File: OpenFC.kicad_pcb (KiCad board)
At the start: 6 copper layers, 29.5 x 29.1 mm, 170 parts, among them J1 5V, J10 5V, J11 5V, J12 5V, J13 5V, J14 5V, J15 5V, J16 5V, J17 5V, J18 5V, J19 5V, J2 5V, J20 5V, J21 5V, J22 5V, J23 5V, J24 5V, J25 5V, J26 5V, J27 5V, J28 5V, J29 5V, J3 5V, J30 5V, J31 5V, J32 5V, J33 5V, J34 5V, J35 5V, J36 5V, J37 5V, J38 5V, J39 5V, J4 5V, J40 5V, J41 5V, J42 5V, J43 5V, J44 5V, J45 5V, J46 5V, J47 5V, J48 5V, J5 5V, J53 5V, J54 5V, J55 5V, J56 5V, J57 5V, J59 5V, J6 5V, J7 5V, J8 5V, J9 5V, P1 SM08B-SRSS-TB(LF)(SN), Q7 DMN1150UFB-7B, SW1 B3U-1000P, U1 SM06B-SRSS-TB(LF)(SN), U10 TLV75533PDBVR, U11 RP2350A_C42411118, U12 ABM8-272-T3_C20625731, U13 W25Q32RVXHJQ TR, U14 LSM6DSV16XTR, U15 XL-1010RGBC-WS2812B, U16 XL-1010RGBC-WS2812B, U17 XL-1010RGBC-WS2812B, U18 XL-1010RGBC-WS2812B, U19 ESP8285H16, U2 W25Q128JVPIQTR, U20 SX1281IMLTRT, U3 XL-1010RGBC-WS2812B, U4 XL-1010RGBC-WS2812B, U5 XL-1010RGBC-WS2812B, U6 LMR51420YDDCR, U7 LMR51420YDDCR, U8 XL-1010RGBC-WS2812B, U9 TLV75533PDBVR, X1 XTM20026000FT00351005

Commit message: First routing
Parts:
- removed D2, D4: LED_1_Green, LED_SMD:LED_0603_1608Metric
- removed J10, J12, J54, J55, J56, J57, J9: 5V, lib:small_pad
- removed R4, R53: 30R, Resistor_SMD:R_0402_1005Metric
- D18, R32: moved to F.Cu
- D3, R3: moved to B.Cu
- moved D1 60.5 mm to (56.8, 102.8)
- moved R29 58.0 mm to (56.4, 104.5), turned to 90 degrees
- moved C40 53.5 mm to (65.0, 107.8), turned to -90 degrees
- moved D3 50.2 mm to (69.4, 122.3), turned to 90 degrees
- moved R3 49.7 mm to (69.7, 119.8), turned to 90 degrees
- moved R32 47.6 mm to (69.1, 107.2)
- moved U17 40.3 mm to (73.6, 124.3), turned to -155 degrees
- moved U18 37.9 mm to (75.9, 121.9), turned to 155 degrees
- moved U3 36.5 mm to (75.9, 101.0), turned to 25 degrees
- moved U4 33.3 mm to (73.6, 98.6), turned to -25 degrees
- moved J40 31.7 mm to (62.0, 105.0), turned to 90 degrees
- moved U15 30.3 mm to (50.2, 121.9), turned to -155 degrees
- moved U16 30.2 mm to (52.6, 124.3), turned to 155 degrees
- moved J8 29.3 mm to (53.0, 118.5)
- moved J7 29.2 mm to (53.0, 116.5)
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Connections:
- U11 pad 4: /RP2350A/ESP8285_EN -> /ELRS/ESP8285_EN
- U11 pad 5: /RP2350A/ESP8285_RST -> /ELRS/ESP8285_RST
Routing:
- net +4.5V: track 0.00 -> 63.5 mm, vias 0 -> 19
- net +BATT: track 0.00 -> 60.4 mm, vias 0 -> 18
- net /LED: track 0.00 -> 59.6 mm, vias 0 -> 6
- net /UART1_RX: track 0.50 -> 53.8 mm, vias 0 -> 2
- net /UART1_TX: track 0.00 -> 47.5 mm, vias 0 -> 3
- net GND: track 3.83 -> 49.1 mm, vias 1 -> 98
- net +3.3V: track 23.7 -> 66.2 mm, vias 6 -> 27
- net +12V: track 0.00 -> 39.7 mm, vias 0 -> 9
- net +1.1V: track 6.68 -> 39.4 mm, vias 1 -> 5
- net /PADS/M4: track 0.00 -> 32.4 mm, vias 0 -> 4
- net /PADS/M2: track 0.00 -> 31.1 mm, vias 0 -> 2
- net /PADS/CURRENT: track 0.00 -> 30.9 mm, vias 0 -> 3
- net /PADS/ESC_TELEM: track 0.00 -> 29.1 mm, vias 0 -> 4
- net /ELRS/ESP8285_RST: track 1.05 -> 28.6 mm, vias 0 -> 3
- net /PADS/M3: track 0.00 -> 26.4 mm, vias 0 -> 4
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- added copper zone on B.Cu, net +12V
- added copper zone on In3.Cu, net +12V
- added copper zone on In4.Cu, net +12V
- added copper zone on B.Cu, net +3.3V
- added copper zone on In4.Cu, net +3.3V
- added copper zone on In3.Cu, net +4.5V
- added copper zone on B.Cu, net +5V
- added copper zone on In2.Cu, net +5V
- added copper zone on B.Cu, net +BATT
- added copper zone on F.Cu, net +BATT
- added copper zone on B.Cu, net GND
- added copper zone on F.Cu, net GND
- added copper zone on In1.Cu, net GND
- added copper zone on In2.Cu, net GND
- added copper zone on In3.Cu, net GND
- added copper zone on In4.Cu, net GND
- added copper zone on B.Cu, net Net-(U6-SW)
- added copper zone on B.Cu, net Net-(U7-SW)
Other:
- outline, holes or cut-outs redrawn

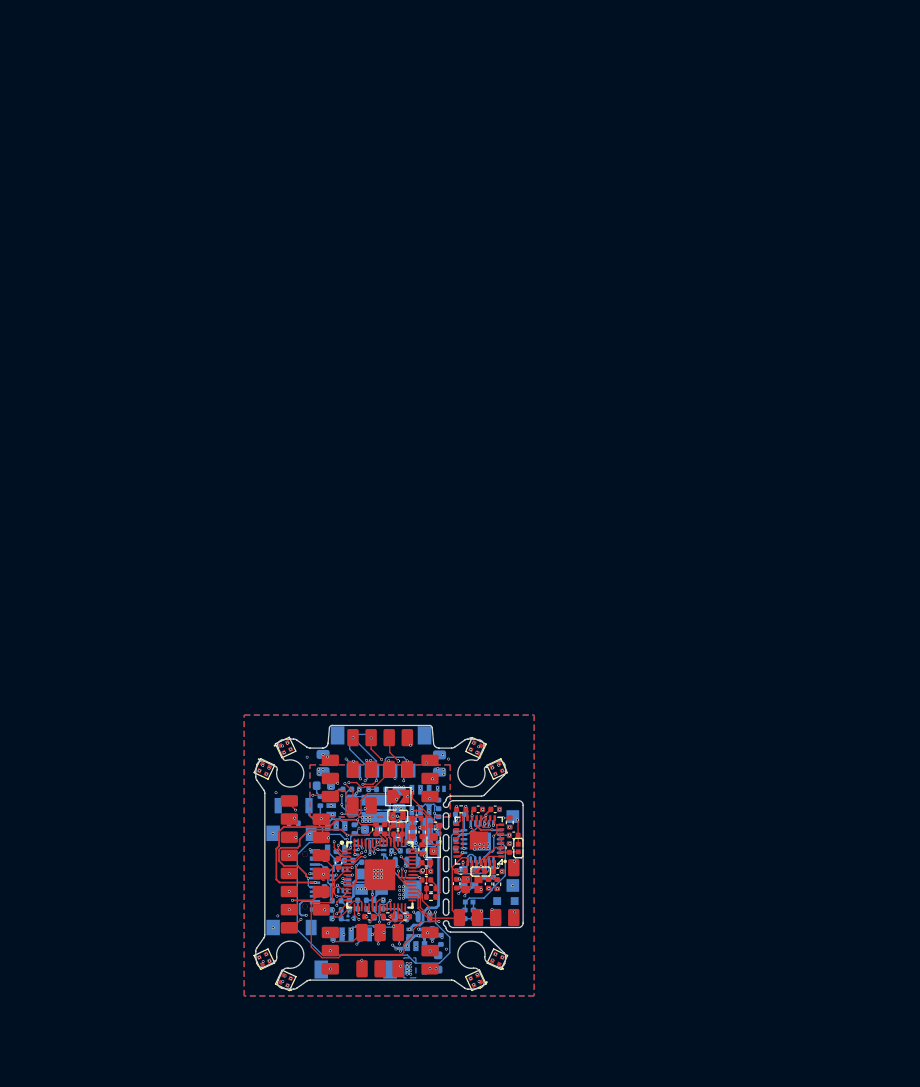
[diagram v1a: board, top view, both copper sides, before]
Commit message: Revised routing. All logic is routed just need uart and power planes
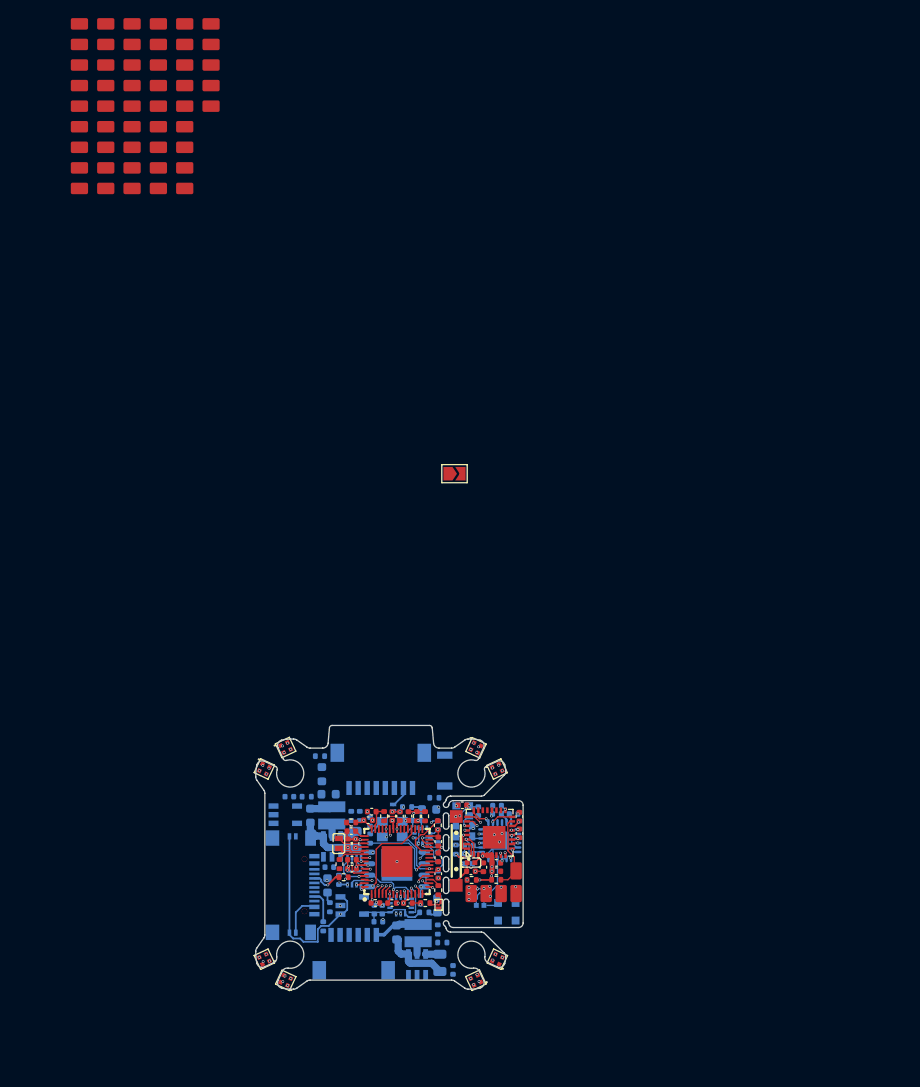
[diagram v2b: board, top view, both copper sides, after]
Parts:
- removed C107: 100n, Capacitor_SMD:C_0402_1005Metric
- removed C16: 4.7uF 50v, Capacitor_SMD:C_0805_2012Metric
- added C111: 100n, Capacitor_SMD:C_0402_1005Metric, B.Cu at (69.4, 107.2)
- added D2: LED_1_Green, LED_SMD:LED_0603_1608Metric, B.Cu at (68.4, 105.4)
- added D4: LED_1_Green, LED_SMD:LED_0603_1608Metric, B.Cu at (69.3, 116.0)
- added J10: 5V, lib:small_pad, F.Cu at (32.7, 18.7)
- added J12: 5V, lib:small_pad, F.Cu at (32.7, 23.3)
- added J54: 5V, lib:small_pad, F.Cu at (44.3, 18.7)
- added J55: 5V, lib:small_pad, F.Cu at (44.3, 21.0)
- added J56: 5V, lib:small_pad, F.Cu at (44.3, 23.3)
- added J57: 5V, lib:small_pad, F.Cu at (44.3, 25.5)
- added J58: 5V, lib:small_pad, F.Cu at (44.3, 27.8)
- added J9: 5V, lib:small_pad, F.Cu at (29.8, 36.9)
- added R4: 30R, Resistor_SMD:R_0402_1005Metric, B.Cu at (67.9, 116.8)
- added R53: 30R, Resistor_SMD:R_0402_1005Metric, B.Cu at (66.0, 105.2)
- added U30: BMP388, lib:SENSORM-SMD_BMP388, B.Cu at (67.7, 108.3)
- C100, C46, C47, C48, C8, C97, C98, C99, L13, Q7, R40, R49, R5: moved to F.Cu
- C13, C18, D18, L8, R1, R2, R32, R7, X1: moved to B.Cu
- moved J28 106.7 mm to (38.5, 18.7), turned to 0 degrees
- moved J29 104.9 mm to (38.5, 21.0), turned to 0 degrees
- moved J19 104.6 mm to (35.6, 18.7)
- moved J20 104.3 mm to (35.6, 21.0)
- moved J35 101.0 mm to (38.5, 25.5), turned to 0 degrees
- moved J30 97.6 mm to (38.5, 23.3)
- moved J41 97.0 mm to (41.4, 18.7), turned to 0 degrees
- moved J16 95.6 mm to (32.7, 32.3), turned to 0 degrees
- moved J17 95.4 mm to (32.7, 34.6), turned to 0 degrees
- moved J36 95.0 mm to (38.5, 27.8), turned to 0 degrees
- moved J42 92.7 mm to (41.4, 21.0), turned to 0 degrees
- moved J37 92.2 mm to (38.5, 30.1), turned to 0 degrees
- moved J18 89.6 mm to (32.7, 36.9), turned to 0 degrees
- moved J38 89.5 mm to (38.5, 32.3), turned to 0 degrees
- moved J11 88.7 mm to (32.7, 21.0)
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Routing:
- net /LED: track 59.6 -> 0.00 mm, vias 6 -> 0
- net +BATT: track 60.4 -> 5.78 mm, vias 18 -> 0
- net /UART1_RX: track 53.8 -> 9.88 mm
- net +4.5V: track 63.5 -> 21.7 mm, vias 19 -> 9
- net /UART1_TX: track 47.5 -> 10.8 mm, vias 3 -> 2
- net +12V: track 39.7 -> 4.45 mm, vias 9 -> 0
- net +1.1V: track 39.4 -> 7.66 mm, vias 5 -> 3
- net /PADS/M4: track 32.4 -> 0.85 mm, vias 4 -> 1
- net /PADS/CURRENT: track 30.9 -> 0.00 mm, vias 3 -> 1
- net /PADS/M2: track 31.1 -> 0.46 mm, vias 2 -> 1
- net /PADS/ESC_TELEM: track 29.1 -> 0.00 mm, vias 4 -> 0
- net +3.3V: track 66.2 -> 38.4 mm, vias 27 -> 25
- net /PADS/M3: track 26.4 -> 0.41 mm, vias 4 -> 1
- net /PADS/M1: track 25.3 -> 1.02 mm, vias 4 -> 1
- net /PADS/PIOUART0_RX: track 23.4 -> 0.00 mm, vias 2 -> 0
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- removed copper zone on B.Cu, net +12V
- removed copper zone on In3.Cu, net +12V
- removed copper zone on In4.Cu, net +12V
- removed copper zone on B.Cu, net +3.3V
- removed copper zone on In4.Cu, net +3.3V
- removed copper zone on In3.Cu, net +4.5V
- removed copper zone on B.Cu, net +5V
- removed copper zone on In2.Cu, net +5V
- removed copper zone on B.Cu, net +BATT
- removed copper zone on F.Cu, net +BATT
- removed copper zone on B.Cu, net GND
- removed copper zone on F.Cu, net GND
- removed copper zone on In1.Cu, net GND
- removed copper zone on In2.Cu, net GND
- removed copper zone on In3.Cu, net GND
- removed copper zone on In4.Cu, net GND
- removed copper zone on B.Cu, net Net-(U6-SW)
- removed copper zone on B.Cu, net Net-(U7-SW)
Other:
- copper layers 6 -> 8

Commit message: almost finished routing
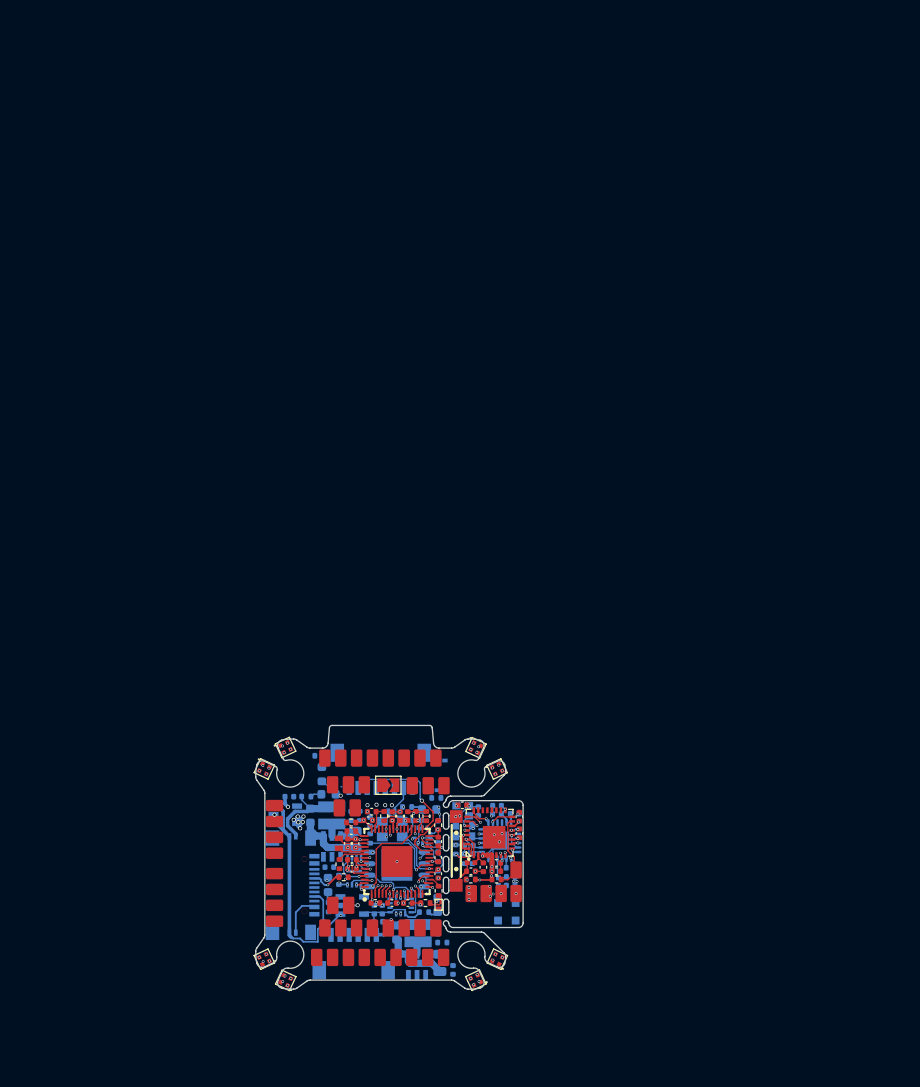
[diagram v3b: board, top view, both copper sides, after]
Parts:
- removed C108: 100nF, Capacitor_SMD:C_0402_1005Metric
- removed C6: 10nF, Capacitor_SMD:C_0402_1005Metric
- removed D18: LED_1_Green, LED_SMD:LED_0603_1608Metric
- removed J10, J11, J12, J54, J55, J58, J9: 5V, lib:small_pad
- removed R27, R30: 100k, Resistor_SMD:R_0402_1005Metric
- removed R32: 200, Resistor_SMD:R_0402_1005Metric
- removed R40, R51: 10k, Resistor_SMD:R_0402_1005Metric
- removed R43, R49: 1k, Resistor_SMD:R_0402_1005Metric
- removed SW1: B3U-1000P, lib:KEY-SMD_B3U-1000PM
- added C1: 10nF, Capacitor_SMD:C_0402_1005Metric, B.Cu at (77.8, 105.9)
- added C2: 100n, Capacitor_SMD:C_0402_1005Metric, F.Cu at (66.0, 106.2)
- added D5: LED_1_Green, LED_SMD:LED_0603_1608Metric, B.Cu at (57.2, 113.8)
- added R10: 10k, Resistor_SMD:R_0402_1005Metric, F.Cu at (69.4, 107.2)
- added R11: 10k, Resistor_SMD:R_0402_1005Metric, F.Cu at (67.0, 106.2)
- added R12: 10k, Resistor_SMD:R_0402_1005Metric, B.Cu at (69.2, 104.2)
- added R13: 1k, Resistor_SMD:R_0402_1005Metric, F.Cu at (69.5, 114.4)
- added R14: 100k, Resistor_SMD:R_0402_1005Metric, B.Cu at (69.4, 118.7)
- added R15: 200R, Resistor_SMD:R_0402_1005Metric, B.Cu at (54.9, 104.0)
- added R16: 100k, Resistor_SMD:R_0402_1005Metric, B.Cu at (59.8, 106.2)
- added R9: 10k, Resistor_SMD:R_0402_1005Metric, B.Cu at (77.4, 111.8)
- added U21: TS2306A 240GF MSM 9_C2976675, lib:SW-SMD_4P-L3.0-W2.0-P0.85-LS3.5, B.Cu at (69.7, 101.7)
- R3, R4: value 30R -> 33R
- moved J19 108.6 mm to (70.0, 121.8), turned to -90 degrees
- moved J28 106.3 mm to (64.8, 121.8), turned to -90 degrees
- moved J20 105.9 mm to (68.2, 121.8), turned to -90 degrees
- moved J29 103.7 mm to (63.0, 121.8), turned to -90 degrees
- moved J21 103.2 mm to (66.5, 121.8), turned to -90 degrees
- moved J41 102.3 mm to (63.9, 118.5), turned to 90 degrees
- moved J42 100.5 mm to (65.7, 118.5), turned to 90 degrees
- moved J35 98.9 mm to (61.2, 121.8), turned to -90 degrees
- moved J43 98.7 mm to (67.4, 118.5), turned to 90 degrees
- moved J30 97.7 mm to (60.4, 118.5), turned to 90 degrees
- moved J44 97.0 mm to (69.2, 118.5), turned to 90 degrees
- moved J36 96.3 mm to (59.5, 121.8), turned to -90 degrees
- moved J22 95.4 mm to (56.9, 118.5), turned to 90 degrees
- moved J37 93.7 mm to (57.8, 121.8), turned to -90 degrees
- moved J23 93.6 mm to (58.7, 118.5), turned to 90 degrees
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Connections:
- J59 pad 1: /ELRS/ESP8285_RST -> /ELRS/ESP_BOOT0
- R29 pad 2: Net-(D1-A) -> Net-(D5-A)
- R3 pad 1: Net-(D3-A) -> +3.3V
- R3 pad 2: +3.3V -> Net-(D3-A)
- R4 pad 1: Net-(D4-A) -> +3.3V_GYRO
- R4 pad 2: +3.3V_GYRO -> Net-(D4-A)
- R6 pad 2: /ELRS/ESP8285_RST -> /ELRS/ESP8285_EN
- R8 pad 2: /ELRS/ESP8285_EN -> /ELRS/ESP_BOOT0
- U11 pad 5: /ELRS/ESP8285_RST -> /ELRS/ESP_BOOT0
- U19 pad 15: /ELRS/ESP8285_RST -> /ELRS/ESP_BOOT0
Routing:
- net /PADS/M4: track 0.85 -> 22.8 mm, vias 1 -> 2
- net +4.5V: track 21.7 -> 39.1 mm
- net /PADS/M3: track 0.41 -> 15.8 mm, vias 1 -> 2
- net /PADS/ESC_TELEM: track 0.00 -> 14.0 mm, vias 0 -> 1
- net /PADS/M2: track 0.46 -> 13.2 mm, vias 1 -> 2
- net GND: track 55.6 -> 67.5 mm, vias 58 -> 60
- net /PADS/M1: track 1.02 -> 11.3 mm, vias 1 -> 2
- net /UART1_TX: track 10.8 -> 20.3 mm, vias 2 -> 3
- net /ELRS/ESP_BOOT0: track 0.00 -> 9.26 mm, vias 0 -> 1
- net /ELRS/ESP8285_RST: track 9.26 -> 0.00 mm, vias 1 -> 0
- net /UART1_RX: track 9.88 -> 17.4 mm, vias 2 -> 3
- net +5V: track 2.44 -> 9.42 mm
- net +3.3V: track 38.4 -> 42.6 mm, vias 25 -> 32
- net Net-(U20-RFIO): track 6.89 -> 3.13 mm
- net +BATT: track 5.78 -> 7.19 mm
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- added copper zone on In1.Cu, net GND
- added copper zone on In6.Cu, net GND

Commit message: Final routing
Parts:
- removed J56: 5V, lib:small_pad
- added J9: 5V, lib:small_pad, F.Cu at (54.2, 109.2)
- added U22: XL-1010RGBC-WS2812B, lib:LED-SMD_4P-L1.0-W1.0-TL_XL-1010RGBC-WS2812B, B.Cu at (75.9, 101.0)
- added U23: XL-1010RGBC-WS2812B, lib:LED-SMD_4P-L1.0-W1.0-TL_XL-1010RGBC-WS2812B, B.Cu at (73.6, 98.6)
- added U24: XL-1010RGBC-WS2812B, lib:LED-SMD_4P-L1.0-W1.0-TL_XL-1010RGBC-WS2812B, B.Cu at (52.6, 98.6)
- added U25: XL-1010RGBC-WS2812B, lib:LED-SMD_4P-L1.0-W1.0-TL_XL-1010RGBC-WS2812B, B.Cu at (50.2, 100.9)
- added U26: XL-1010RGBC-WS2812B, lib:LED-SMD_4P-L1.0-W1.0-TL_XL-1010RGBC-WS2812B, B.Cu at (50.2, 122.0)
- added U27: XL-1010RGBC-WS2812B, lib:LED-SMD_4P-L1.0-W1.0-TL_XL-1010RGBC-WS2812B, B.Cu at (52.6, 124.3)
- added U28: XL-1010RGBC-WS2812B, lib:LED-SMD_4P-L1.0-W1.0-TL_XL-1010RGBC-WS2812B, B.Cu at (73.6, 124.3)
- added U29: XL-1010RGBC-WS2812B, lib:LED-SMD_4P-L1.0-W1.0-TL_XL-1010RGBC-WS2812B, B.Cu at (75.9, 121.9)
- moved J6 13.1 mm to (51.2, 118.1), turned to 0 degrees
- moved J48 13.0 mm to (51.2, 104.8), turned to 180 degrees
- moved J5 9.60 mm to (51.2, 116.3), turned to 0 degrees
- moved J47 9.45 mm to (51.2, 106.5), turned to 180 degrees
- moved J57 6.47 mm to (54.1, 107.4), turned to 180 degrees
- moved J7 6.10 mm to (51.2, 114.6), turned to 180 degrees
- moved J46 5.95 mm to (51.2, 108.3), turned to 180 degrees
- moved J40 5.90 mm to (54.1, 113.7), turned to 180 degrees
- moved C36 5.79 mm to (65.2, 123.2)
- moved J39 3.72 mm to (54.1, 115.5), turned to 180 degrees
- moved J8 2.60 mm to (51.2, 112.8), turned to 180 degrees
- moved J45 2.45 mm to (51.2, 110.0), turned to 180 degrees
- moved J22 1.90 mm to (57.0, 120.4)
- moved J23 1.90 mm to (58.8, 120.4)
- moved J30 1.90 mm to (60.5, 120.4)
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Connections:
- U18 pad 1: unconnected-(U18-DOUT-Pad1) -> Net-(U18-DOUT)
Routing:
- net +4.5V: track 39.1 -> 135.7 mm, vias 9 -> 11
- net +BATT: track 7.19 -> 68.9 mm, vias 0 -> 11
- net /LED: track 0.00 -> 48.9 mm, vias 0 -> 2
- net +3.3V: track 42.6 -> 76.8 mm, vias 32 -> 34
- net /PADS/BUZZER-: track 0.00 -> 29.2 mm, vias 0 -> 2
- net Net-(U11-QSPI_SS): track 1.07 -> 30.0 mm, vias 1 -> 2
- net +5V: track 9.42 -> 38.0 mm, vias 0 -> 20
- net /ELRS/ESP_BOOT0: track 9.26 -> 33.0 mm, vias 1 -> 2
- net +1.1V: track 7.75 -> 31.0 mm
- net Net-(U15-DIN): track 0.00 -> 22.7 mm
- net /UART1_RX: track 17.4 -> 38.8 mm, vias 3 -> 4
- net Net-(U16-DOUT): track 0.00 -> 21.0 mm
- net Net-(U23-DIN): track 0.00 -> 20.6 mm
- net /I2C_SDA: track 3.84 -> 22.9 mm, vias 1 -> 2
- net /UART1_TX: track 20.3 -> 38.9 mm, vias 3 -> 4
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- added copper zone on In3.Cu, net +3.3V
- added copper zone on In4.Cu, net +3.3V_GYRO
- added copper zone on In3.Cu, net +5V
- added copper zone on B.Cu, net GND
- added copper zone on F.Cu, net GND
- added copper zone on In2.Cu, net GND
- added copper zone on In4.Cu, net GND
- added copper zone on In5.Cu, net GND
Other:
- board size 29.5 x 29.1 mm -> 29.5 x 27.6 mm
- board text added: "+"
- board text added: "+12v"
- board text added: "+3.3 imu"
- board text added: "+3.3v"
- board text added: "+5v"
- board text added: "1"
- board text added: "12v"
- board text added: "2"
- board text added: "3"
- board text added: "3.3V"
- board text added: "4"
- board text added: "ADC"
- board text added: "B = SIGNAL"
- board text added: "C"
- board text added: "F = SIGNAL"
- board text added: "GND"
- board text added: "Keep Out"
- board text added: "LN1 = GROUND (F Reference)"
- board text added: "LN2 = X-SIGNALS"
- board text added: "LN3 = PWR (5v/3.3v)"
- board text added: "LN4 = GND"
- board text added: "LN5 = Y-SIGNALS"
- board text added: "LN6 = GROUND (B Reference)"
- board text added: "RX"
- board text added: "RX0"
- board text added: "RX1"
- board text added: "RX2"
- board text added: "SCL"
- board text added: "SDA"
- board text added: "TX"
- board text added: "TX0"
- board text added: "TX1"
- board text added: "Tx2"
- board text added: "boot"
- board text added: "break me"
- board text added: "buz+"
- board text added: "buz-"
- board text added: "gnd"
- board text added: "i2c"
- board text added: "led"
- board text added: "led bridge"
- board text added: "sbus"
- board text added: "status"
- board text added: "t"

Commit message: ESP XTAL routed with 1 via
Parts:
- C19: moved to B.Cu
- moved C19 4.74 mm to (71.7, 109.7)
- moved C18 2.79 mm to (71.0, 105.8)
- moved X1 2.52 mm to (71.6, 108.0), turned to -90 degrees
- moved OSC1 2.32 mm to (72.9, 105.6)
- moved L8 2.15 mm to (73.2, 109.3), turned to 90 degrees
- moved C9 1.18 mm to (72.7, 111.5)
- moved C7 1.18 mm to (72.8, 110.6)
- moved R7 1.18 mm to (71.3, 111.0)
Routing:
- net /UART1_TX: track 38.9 -> 35.2 mm
- net /UART1_RX: track 38.8 -> 35.7 mm
- net Net-(L8-Pad2): track 5.18 -> 2.21 mm
- net /ELRS/RADIO_OSC: track 1.26 -> 3.13 mm
- net GND: track 83.7 -> 82.2 mm, vias 139 -> 138
- net Net-(U20-VR_PA): track 1.02 -> 1.79 mm
- net Net-(U19-XTAL_IN): track 3.98 -> 3.30 mm, vias 2 -> 1
- net +3.3V: track 76.8 -> 77.4 mm
